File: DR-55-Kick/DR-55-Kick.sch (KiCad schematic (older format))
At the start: 19 parts

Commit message: Values
Added Values to all components
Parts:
- C? (x4): value C -> .068
- C?: value C -> .047
- C?: value C -> .027
- R?: value R -> 680k
- R? (x4): value R -> 22k
- R?: value R -> 2.2M
- R?: value R -> 10k
- R?: value R -> 220k
- R?: value R -> 1k
- R?: value R -> 150k
- R?: value R -> 820
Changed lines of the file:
@@
 $Descr A4 11693 8268
 encoding utf-8
-Sheet 7 7
+Sheet 6 7
 Title ""
 Date ""
@@
 P 2250 1500
 F 0 "R?" V 2043 1500 50  0000 C CNN
-F 1 "R" V 2134 1500 50  0000 C CNN
+F 1 "680k" V 2134 1500 50  0000 C CNN
 F 2 "" V 2180 1500 50  0001 C CNN
 F 3 "~" H 2250 1500 50  0001 C CNN
@@
 P 2500 2000
 F 0 "C?" H 2615 2046 50  0000 L CNN
-F 1 "C" H 2615 1955 50  0000 L CNN
+F 1 ".068" H 2615 1955 50  0000 L CNN
 F 2 "" H 2538 1850 50  0001 C CNN
 F 3 "~" H 2500 2000 50  0001 C CNN
@@
 P 2250 2500
 F 0 "C?" H 2365 2546 50  0000 L CNN
-F 1 "C" H 2365 2455 50  0000 L CNN
+F 1 ".068" H 2365 2455 50  0000 L CNN
 F 2 "" H 2288 2350 50  0001 C CNN
 F 3 "~" H 2250 2500 50  0001 C CNN
@@
 P 2750 2500
 F 0 "C?" H 2865 2546 50  0000 L CNN
-F 1 "C" H 2865 2455 50  0000 L CNN
+F 1 ".068" H 2865 2455 50  0000 L CNN
 F 2 "" H 2788 2350 50  0001 C CNN
 F 3 "~" H 2750 2500 50  0001 C CNN
@@
 P 2000 2750
 F 0 "R?" V 1793 2750 50  0000 C CNN
-F 1 "R" V 1884 2750 50  0000 C CNN
+F 1 "22k" V 1884 2750 50  0000 C CNN
 F 2 "" V 1930 2750 50  0001 C CNN
 F 3 "~" H 2000 2750 50  0001 C CNN
@@
 P 2500 2750
 F 0 "R?" V 2293 2750 50  0000 C CNN
-F 1 "R" V 2384 2750 50  0000 C CNN
+F 1 "22k" V 2384 2750 50  0000 C CNN
 F 2 "" V 2430 2750 50  0001 C CNN
 F 3 "~" H 2500 2750 50  0001 C CNN
@@
 P 3000 2750
 F 0 "R?" V 2793 2750 50  0000 C CNN
-F 1 "R" V 2884 2750 50  0000 C CNN
+F 1 "22k" V 2884 2750 50  0000 C CNN
 F 2 "" V 2930 2750 50  0001 C CNN
 F 3 "~" H 3000 2750 50  0001 C CNN
@@
 P 3250 2500
 F 0 "C?" H 3365 2546 50  0000 L CNN
-F 1 "C" H 3365 2455 50  0000 L CNN
+F 1 ".068" H 3365 2455 50  0000 L CNN
 F 2 "" H 3288 2350 50  0001 C CNN
 F 3 "~" H 3250 2500 50  0001 C CNN
@@
 P 3500 2250
 F 0 "R?" V 3293 2250 50  0000 C CNN
-F 1 "R" V 3384 2250 50  0000 C CNN
+F 1 "2.2M" V 3384 2250 50  0000 C CNN
 F 2 "" V 3430 2250 50  0001 C CNN
 F 3 "~" H 3500 2250 50  0001 C CNN
@@
 P 4000 1750
 F 0 "R?" V 3793 1750 50  0000 C CNN
-F 1 "R" V 3884 1750 50  0000 C CNN
+F 1 "10k" V 3884 1750 50  0000 C CNN
 F 2 "" V 3930 1750 50  0001 C CNN
 F 3 "~" H 4000 1750 50  0001 C CNN
@@
 P 4750 2500
 F 0 "C?" H 4865 2546 50  0000 L CNN
-F 1 "C" H 4865 2455 50  0000 L CNN
+F 1 ".047" H 4865 2455 50  0000 L CNN
 F 2 "" H 4788 2350 50  0001 C CNN
 F 3 "~" H 4750 2500 50  0001 C CNN
@@
 P 5000 2250
 F 0 "R?" V 4793 2250 50  0000 C CNN
-F 1 "R" V 4884 2250 50  0000 C CNN
+F 1 "220k" V 4884 2250 50  0000 C CNN
 F 2 "" V 4930 2250 50  0001 C CNN
 F 3 "~" H 5000 2250 50  0001 C CNN
@@
 P 5500 3250
 F 0 "R?" V 5293 3250 50  0000 C CNN
-F 1 "R" V 5384 3250 50  0000 C CNN
+F 1 "1k" V 5384 3250 50  0000 C CNN
 F 2 "" V 5430 3250 50  0001 C CNN
 F 3 "~" H 5500 3250 50  0001 C CNN
@@
 P 5500 1750
 F 0 "R?" V 5293 1750 50  0000 C CNN
-F 1 "R" V 5384 1750 50  0000 C CNN
+F 1 "22k" V 5384 1750 50  0000 C CNN
 F 2 "" V 5430 1750 50  0001 C CNN
 F 3 "~" H 5500 1750 50  0001 C CNN
@@
 P 6000 2250
 F 0 "R?" V 5793 2250 50  0000 C CNN
-F 1 "R" V 5884 2250 50  0000 C CNN
+F 1 "150k" V 5884 2250 50  0000 C CNN
 F 2 "" V 5930 2250 50  0001 C CNN
 F 3 "~" H 6000 2250 50  0001 C CNN
@@
 P 6000 2750
 F 0 "C?" H 6115 2796 50  0000 L CNN
-F 1 "C" H 6115 2705 50  0000 L CNN
+F 1 ".027" H 6115 2705 50  0000 L CNN
 F 2 "" H 6038 2600 50  0001 C CNN
 F 3 "~" H 6000 2750 50  0001 C CNN
@@
 P 4000 3250
 F 0 "R?" V 3793 3250 50  0000 C CNN
-F 1 "R" V 3884 3250 50  0000 C CNN
+F 1 "820" V 3884 3250 50  0000 C CNN
 F 2 "" V 3930 3250 50  0001 C CNN
 F 3 "~" H 4000 3250 50  0001 C CNN

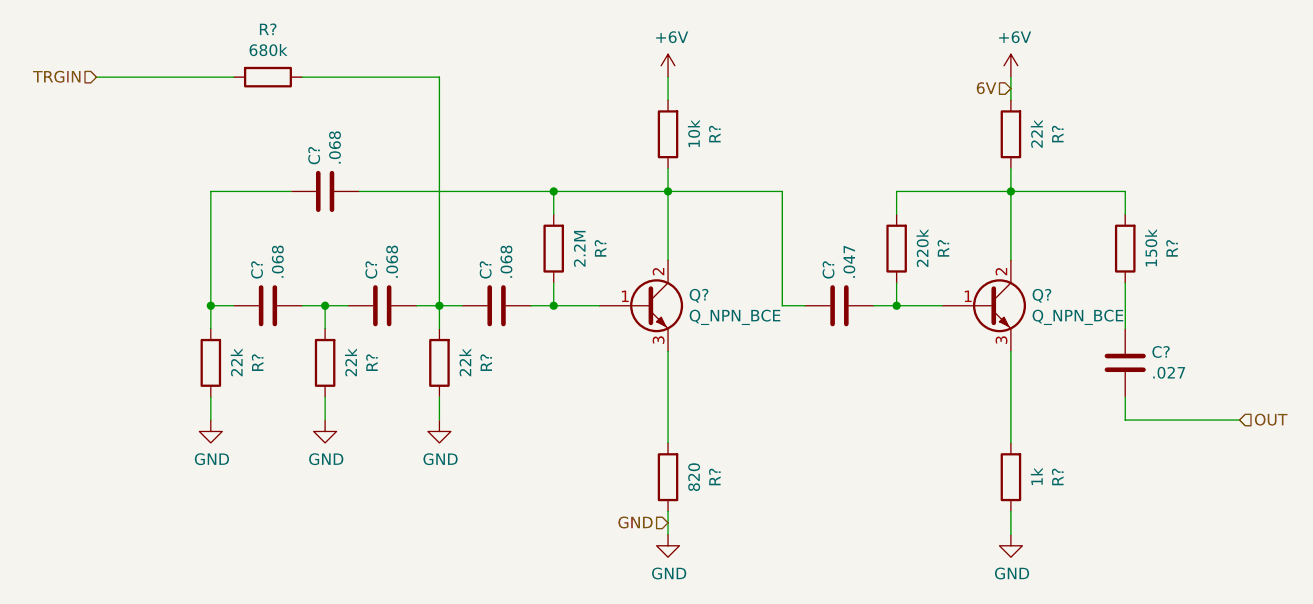
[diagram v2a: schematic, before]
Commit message: Resistor enumeration
All resistors, diodes and transistors get numbers
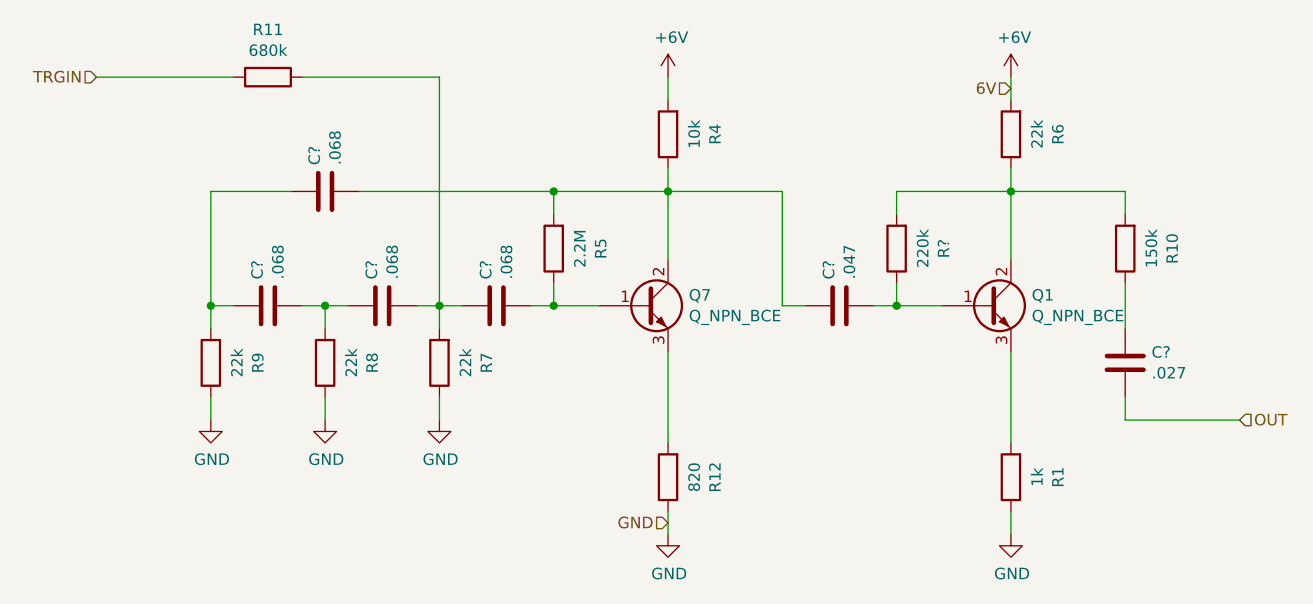
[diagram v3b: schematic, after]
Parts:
- gave numbers to parts that had none: 12
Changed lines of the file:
@@
 $Descr A4 11693 8268
 encoding utf-8
-Sheet 6 7
+Sheet 5 7
 Title ""
 Date ""
@@
 $EndDescr
 $Comp
-L Device:R R?
+L Device:R R11
 U 1 1 626D5822
 P 2250 1500
-F 0 "R?" V 2043 1500 50  0000 C CNN
+F 0 "R11" V 2043 1500 50  0000 C CNN
 F 1 "680k" V 2134 1500 50  0000 C CNN
 F 2 "" V 2180 1500 50  0001 C CNN
@@
 $EndComp
 $Comp
-L Device:Q_NPN_BCE Q?
+L Device:Q_NPN_BCE Q7
 U 1 1 626DA6FA
 P 3900 2500
-F 0 "Q?" H 4091 2546 50  0000 L CNN
+F 0 "Q7" H 4091 2546 50  0000 L CNN
 F 1 "Q_NPN_BCE" H 4091 2455 50  0000 L CNN
 F 2 "" H 4100 2600 50  0001 C CNN
@@
 $EndComp
 $Comp
-L Device:R R?
+L Device:R R9
 U 1 1 626DD721
 P 2000 2750
-F 0 "R?" V 1793 2750 50  0000 C CNN
+F 0 "R9" V 1793 2750 50  0000 C CNN
 F 1 "22k" V 1884 2750 50  0000 C CNN
 F 2 "" V 1930 2750 50  0001 C CNN
@@
 $EndComp
 $Comp
-L Device:R R?
+L Device:R R8
 U 1 1 626DD93D
 P 2500 2750
-F 0 "R?" V 2293 2750 50  0000 C CNN
+F 0 "R8" V 2293 2750 50  0000 C CNN
 F 1 "22k" V 2384 2750 50  0000 C CNN
 F 2 "" V 2430 2750 50  0001 C CNN
@@
 $EndComp
 $Comp
-L Device:R R?
+L Device:R R7
 U 1 1 626DDBF5
 P 3000 2750
-F 0 "R?" V 2793 2750 50  0000 C CNN
+F 0 "R7" V 2793 2750 50  0000 C CNN
 F 1 "22k" V 2884 2750 50  0000 C CNN
 F 2 "" V 2930 2750 50  0001 C CNN
@@
 $EndComp
 $Comp
-L Device:R R?
+L Device:R R5
 U 1 1 626DE42E
 P 3500 2250
-F 0 "R?" V 3293 2250 50  0000 C CNN
+F 0 "R5" V 3293 2250 50  0000 C CNN
 F 1 "2.2M" V 3384 2250 50  0000 C CNN
 F 2 "" V 3430 2250 50  0001 C CNN
@@
 $EndComp
 $Comp
-L Device:R R?
+L Device:R R4
 U 1 1 626E0253
 P 4000 1750
-F 0 "R?" V 3793 1750 50  0000 C CNN
+F 0 "R4" V 3793 1750 50  0000 C CNN
 F 1 "10k" V 3884 1750 50  0000 C CNN
 F 2 "" V 3930 1750 50  0001 C CNN
@@
 $EndComp
 $Comp
-L Device:Q_NPN_BCE Q?
+L Device:Q_NPN_BCE Q1
 U 1 1 626E0FB1
 P 5400 2500
-F 0 "Q?" H 5591 2546 50  0000 L CNN
+F 0 "Q1" H 5591 2546 50  0000 L CNN
 F 1 "Q_NPN_BCE" H 5591 2455 50  0000 L CNN
 F 2 "" H 5600 2600 50  0001 C CNN
@@
 $EndComp
 $Comp
-L Device:R R?
+L Device:R R1
 U 1 1 626E1441
 P 5500 3250
-F 0 "R?" V 5293 3250 50  0000 C CNN
+F 0 "R1" V 5293 3250 50  0000 C CNN
 F 1 "1k" V 5384 3250 50  0000 C CNN
 F 2 "" V 5430 3250 50  0001 C CNN
@@
 $EndComp
 $Comp
-L Device:R R?
+L Device:R R6
 U 1 1 626E191A
 P 5500 1750
-F 0 "R?" V 5293 1750 50  0000 C CNN
+F 0 "R6" V 5293 1750 50  0000 C CNN
 F 1 "22k" V 5384 1750 50  0000 C CNN
 F 2 "" V 5430 1750 50  0001 C CNN
@@
 $EndComp
 $Comp
-L Device:R R?
+L Device:R R10
 U 1 1 626E1A5C
 P 6000 2250
-F 0 "R?" V 5793 2250 50  0000 C CNN
+F 0 "R10" V 5793 2250 50  0000 C CNN
 F 1 "150k" V 5884 2250 50  0000 C CNN
 F 2 "" V 5930 2250 50  0001 C CNN
@@
 $EndComp
 $Comp
-L Device:R R?
+L Device:R R12
 U 1 1 626EAE52
 P 4000 3250
-F 0 "R?" V 3793 3250 50  0000 C CNN
+F 0 "R12" V 3793 3250 50  0000 C CNN
 F 1 "820" V 3884 3250 50  0000 C CNN
 F 2 "" V 3930 3250 50  0001 C CNN

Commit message: Footprints added
Added most of the footprints for a 0805 SMD PCB. some placeholder footprints added and some missing
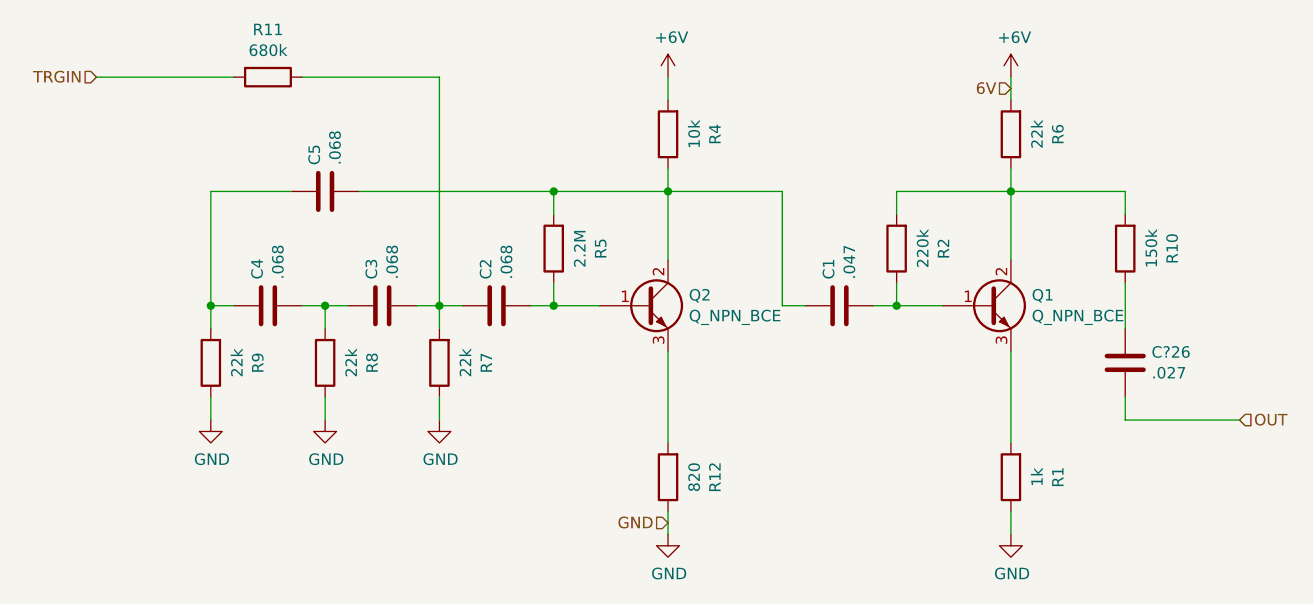
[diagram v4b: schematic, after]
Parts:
- C1, C2, C3, C4, C5, C?26: renamed from C?; footprint (none) -> Capacitor_SMD:C_0805_2012Metric_Pad1.18x1.45mm_HandSolder
- Q1: footprint (none) -> Package_TO_SOT_SMD:SOT-23
- Q2: renamed from Q7; footprint (none) -> Package_TO_SOT_SMD:SOT-23
- R1, R10, R11, R12, R4, R5, R6, R7, R8, R9: footprint (none) -> Resistor_SMD:R_0805_2012Metric_Pad1.20x1.40mm_HandSolder
- R2: renamed from R?; footprint (none) -> Resistor_SMD:R_0805_2012Metric_Pad1.20x1.40mm_HandSolder
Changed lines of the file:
@@
 F 0 "R11" V 2043 1500 50  0000 C CNN
 F 1 "680k" V 2134 1500 50  0000 C CNN
-F 2 "" V 2180 1500 50  0001 C CNN
+F 2 "Resistor_SMD:R_0805_2012Metric_Pad1.20x1.40mm_HandSolder" V 2180 1500 50  0001 C CNN
 F 3 "~" H 2250 1500 50  0001 C CNN
 	1    2250 1500
@@
 $EndComp
 $Comp
-L Device:C C?
+L Device:C C5
 U 1 1 626D8FE5
 P 2500 2000
-F 0 "C?" H 2615 2046 50  0000 L CNN
+F 0 "C5" H 2615 2046 50  0000 L CNN
 F 1 ".068" H 2615 1955 50  0000 L CNN
-F 2 "" H 2538 1850 50  0001 C CNN
+F 2 "Capacitor_SMD:C_0805_2012Metric_Pad1.18x1.45mm_HandSolder" H 2538 1850 50  0001 C CNN
 F 3 "~" H 2500 2000 50  0001 C CNN
 	1    2500 2000
@@
 $EndComp
 $Comp
-L Device:Q_NPN_BCE Q7
+L Device:Q_NPN_BCE Q2
 U 1 1 626DA6FA
 P 3900 2500
-F 0 "Q7" H 4091 2546 50  0000 L CNN
+F 0 "Q2" H 4091 2546 50  0000 L CNN
 F 1 "Q_NPN_BCE" H 4091 2455 50  0000 L CNN
-F 2 "" H 4100 2600 50  0001 C CNN
+F 2 "Package_TO_SOT_SMD:SOT-23" H 4100 2600 50  0001 C CNN
 F 3 "~" H 3900 2500 50  0001 C CNN
 	1    3900 2500
@@
 $EndComp
 $Comp
-L Device:C C?
+L Device:C C4
 U 1 1 626DCEAC
 P 2250 2500
-F 0 "C?" H 2365 2546 50  0000 L CNN
+F 0 "C4" H 2365 2546 50  0000 L CNN
 F 1 ".068" H 2365 2455 50  0000 L CNN
-F 2 "" H 2288 2350 50  0001 C CNN
+F 2 "Capacitor_SMD:C_0805_2012Metric_Pad1.18x1.45mm_HandSolder" H 2288 2350 50  0001 C CNN
 F 3 "~" H 2250 2500 50  0001 C CNN
 	1    2250 2500
@@
 $EndComp
 $Comp
-L Device:C C?
+L Device:C C3
 U 1 1 626DD0C9
 P 2750 2500
-F 0 "C?" H 2865 2546 50  0000 L CNN
+F 0 "C3" H 2865 2546 50  0000 L CNN
 F 1 ".068" H 2865 2455 50  0000 L CNN
-F 2 "" H 2788 2350 50  0001 C CNN
+F 2 "Capacitor_SMD:C_0805_2012Metric_Pad1.18x1.45mm_HandSolder" H 2788 2350 50  0001 C CNN
 F 3 "~" H 2750 2500 50  0001 C CNN
 	1    2750 2500
@@
 F 0 "R9" V 1793 2750 50  0000 C CNN
 F 1 "22k" V 1884 2750 50  0000 C CNN
-F 2 "" V 1930 2750 50  0001 C CNN
+F 2 "Resistor_SMD:R_0805_2012Metric_Pad1.20x1.40mm_HandSolder" V 1930 2750 50  0001 C CNN
 F 3 "~" H 2000 2750 50  0001 C CNN
 	1    2000 2750
@@
 F 0 "R8" V 2293 2750 50  0000 C CNN
 F 1 "22k" V 2384 2750 50  0000 C CNN
-F 2 "" V 2430 2750 50  0001 C CNN
+F 2 "Resistor_SMD:R_0805_2012Metric_Pad1.20x1.40mm_HandSolder" V 2430 2750 50  0001 C CNN
 F 3 "~" H 2500 2750 50  0001 C CNN
 	1    2500 2750
@@
 F 0 "R7" V 2793 2750 50  0000 C CNN
 F 1 "22k" V 2884 2750 50  0000 C CNN
-F 2 "" V 2930 2750 50  0001 C CNN
+F 2 "Resistor_SMD:R_0805_2012Metric_Pad1.20x1.40mm_HandSolder" V 2930 2750 50  0001 C CNN
 F 3 "~" H 3000 2750 50  0001 C CNN
 	1    3000 2750
@@
 $EndComp
 $Comp
-L Device:C C?
+L Device:C C2
 U 1 1 626DE213
 P 3250 2500
-F 0 "C?" H 3365 2546 50  0000 L CNN
+F 0 "C2" H 3365 2546 50  0000 L CNN
 F 1 ".068" H 3365 2455 50  0000 L CNN
-F 2 "" H 3288 2350 50  0001 C CNN
+F 2 "Capacitor_SMD:C_0805_2012Metric_Pad1.18x1.45mm_HandSolder" H 3288 2350 50  0001 C CNN
 F 3 "~" H 3250 2500 50  0001 C CNN
 	1    3250 2500
@@
 F 0 "R5" V 3293 2250 50  0000 C CNN
 F 1 "2.2M" V 3384 2250 50  0000 C CNN
-F 2 "" V 3430 2250 50  0001 C CNN
+F 2 "Resistor_SMD:R_0805_2012Metric_Pad1.20x1.40mm_HandSolder" V 3430 2250 50  0001 C CNN
 F 3 "~" H 3500 2250 50  0001 C CNN
 	1    3500 2250
@@
 F 0 "R4" V 3793 1750 50  0000 C CNN
 F 1 "10k" V 3884 1750 50  0000 C CNN
-F 2 "" V 3930 1750 50  0001 C CNN
+F 2 "Resistor_SMD:R_0805_2012Metric_Pad1.20x1.40mm_HandSolder" V 3930 1750 50  0001 C CNN
 F 3 "~" H 4000 1750 50  0001 C CNN
 	1    4000 1750
@@
 $EndComp
 $Comp
-L Device:C C?
+L Device:C C1
 U 1 1 626E06C5
 P 4750 2500
-F 0 "C?" H 4865 2546 50  0000 L CNN
+F 0 "C1" H 4865 2546 50  0000 L CNN
 F 1 ".047" H 4865 2455 50  0000 L CNN
-F 2 "" H 4788 2350 50  0001 C CNN
+F 2 "Capacitor_SMD:C_0805_2012Metric_Pad1.18x1.45mm_HandSolder" H 4788 2350 50  0001 C CNN
 F 3 "~" H 4750 2500 50  0001 C CNN
 	1    4750 2500
@@
 $EndComp
 $Comp
-L Device:R R?
+L Device:R R2
 U 1 1 626E09DA
 P 5000 2250
-F 0 "R?" V 4793 2250 50  0000 C CNN
+F 0 "R2" V 4793 2250 50  0000 C CNN
 F 1 "220k" V 4884 2250 50  0000 C CNN
-F 2 "" V 4930 2250 50  0001 C CNN
+F 2 "Resistor_SMD:R_0805_2012Metric_Pad1.20x1.40mm_HandSolder" V 4930 2250 50  0001 C CNN
 F 3 "~" H 5000 2250 50  0001 C CNN
 	1    5000 2250
@@
 F 0 "Q1" H 5591 2546 50  0000 L CNN
 F 1 "Q_NPN_BCE" H 5591 2455 50  0000 L CNN
-F 2 "" H 5600 2600 50  0001 C CNN
+F 2 "Package_TO_SOT_SMD:SOT-23" H 5600 2600 50  0001 C CNN
 F 3 "~" H 5400 2500 50  0001 C CNN
 	1    5400 2500
@@
 F 0 "R1" V 5293 3250 50  0000 C CNN
 F 1 "1k" V 5384 3250 50  0000 C CNN
-F 2 "" V 5430 3250 50  0001 C CNN
+F 2 "Resistor_SMD:R_0805_2012Metric_Pad1.20x1.40mm_HandSolder" V 5430 3250 50  0001 C CNN
 F 3 "~" H 5500 3250 50  0001 C CNN
 	1    5500 3250
@@
 F 0 "R6" V 5293 1750 50  0000 C CNN
 F 1 "22k" V 5384 1750 50  0000 C CNN
-F 2 "" V 5430 1750 50  0001 C CNN
+F 2 "Resistor_SMD:R_0805_2012Metric_Pad1.20x1.40mm_HandSolder" V 5430 1750 50  0001 C CNN
 F 3 "~" H 5500 1750 50  0001 C CNN
 	1    5500 1750
@@
 F 0 "R10" V 5793 2250 50  0000 C CNN
 F 1 "150k" V 5884 2250 50  0000 C CNN
-F 2 "" V 5930 2250 50  0001 C CNN
+F 2 "Resistor_SMD:R_0805_2012Metric_Pad1.20x1.40mm_HandSolder" V 5930 2250 50  0001 C CNN
 F 3 "~" H 6000 2250 50  0001 C CNN
 	1    6000 2250
@@
 $EndComp
 $Comp
-L Device:C C?
+L Device:C C?26
 U 1 1 626E2006
 P 6000 2750
-F 0 "C?" H 6115 2796 50  0000 L CNN
+F 0 "C?26" H 6115 2796 50  0000 L CNN
 F 1 ".027" H 6115 2705 50  0000 L CNN
-F 2 "" H 6038 2600 50  0001 C CNN
+F 2 "Capacitor_SMD:C_0805_2012Metric_Pad1.18x1.45mm_HandSolder" H 6038 2600 50  0001 C CNN
 F 3 "~" H 6000 2750 50  0001 C CNN
 	1    6000 2750
@@
 	3000 2500 3100 2500
 $Comp
-L power:GND #PWR?
+L power:GND #PWR0121
 U 1 1 626E85CA
 P 2000 3000
-F 0 "#PWR?" H 2000 2750 50  0001 C CNN
+F 0 "#PWR0121" H 2000 2750 50  0001 C CNN
 F 1 "GND" H 2005 2827 50  0000 C CNN
 F 2 "" H 2000 3000 50  0001 C CNN
@@
 $EndComp
 $Comp
-L power:GND #PWR?
+L power:GND #PWR0122
 U 1 1 626E9E11
 P 2500 3000
-F 0 "#PWR?" H 2500 2750 50  0001 C CNN
+F 0 "#PWR0122" H 2500 2750 50  0001 C CNN
 F 1 "GND" H 2505 2827 50  0000 C CNN
 F 2 "" H 2500 3000 50  0001 C CNN
@@
 $EndComp
 $Comp
-L power:GND #PWR?
+L power:GND #PWR0123
 U 1 1 626EA3BB
 P 3000 3000
-F 0 "#PWR?" H 3000 2750 50  0001 C CNN
+F 0 "#PWR0123" H 3000 2750 50  0001 C CNN
 F 1 "GND" H 3005 2827 50  0000 C CNN
 F 2 "" H 3000 3000 50  0001 C CNN
@@
 F 0 "R12" V 3793 3250 50  0000 C CNN
 F 1 "820" V 3884 3250 50  0000 C CNN
-F 2 "" V 3930 3250 50  0001 C CNN
+F 2 "Resistor_SMD:R_0805_2012Metric_Pad1.20x1.40mm_HandSolder" V 3930 3250 50  0001 C CNN
 F 3 "~" H 4000 3250 50  0001 C CNN
 	1    4000 3250
@@
 $EndComp
 $Comp
-L power:GND #PWR?
+L power:GND #PWR0124
 U 1 1 626EB7AD
 P 4000 3500
-F 0 "#PWR?" H 4000 3250 50  0001 C CNN
+F 0 "#PWR0124" H 4000 3250 50  0001 C CNN
 F 1 "GND" H 4005 3327 50  0000 C CNN
 F 2 "" H 4000 3500 50  0001 C CNN
@@
 $EndComp
 $Comp
-L power:GND #PWR?
+L power:GND #PWR0125
 U 1 1 626EBE12
 P 5500 3500
-F 0 "#PWR?" H 5500 3250 50  0001 C CNN
+F 0 "#PWR0125" H 5500 3250 50  0001 C CNN
 F 1 "GND" H 5505 3327 50  0000 C CNN
 F 2 "" H 5500 3500 50  0001 C CNN
@@
 	2000 3000 2000 2900
 $Comp
-L power:+6V #PWR?
+L power:+6V #PWR0126
 U 1 1 626EEDCC
 P 5500 1500
-F 0 "#PWR?" H 5500 1350 50  0001 C CNN
+F 0 "#PWR0126" H 5500 1350 50  0001 C CNN
 F 1 "+6V" H 5515 1673 50  0000 C CNN
 F 2 "" H 5500 1500 50  0001 C CNN
@@
 $EndComp
 $Comp
-L power:+6V #PWR?
+L power:+6V #PWR0127
 U 1 1 626F016E
 P 4000 1500
-F 0 "#PWR?" H 4000 1350 50  0001 C CNN
+F 0 "#PWR0127" H 4000 1350 50  0001 C CNN
 F 1 "+6V" H 4015 1673 50  0000 C CNN
 F 2 "" H 4000 1500 50  0001 C CNN
